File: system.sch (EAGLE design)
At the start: 24 parts, among them IC1 TPS7B8650BQDDARQ1, J1 163-179PH-EX, J2 TSW-104-07-F-S, U1 ATMEGA328PB-AU

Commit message: Removed redundant V_SIG to ADC line
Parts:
- removed R8: 0, rcl:R-US_R0603
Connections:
- removed net N$11: R8.1, U1.(ADC2/PTCY)PC2
- removed net V_SIG: R8.2
- net N$3: no longer R8.1
- net VS_5V: no longer R8.2
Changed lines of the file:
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@@
 <part name="R7" library="rcl" library_urn="urn:adsk.eagle:library:334" deviceset="R-US_" device="R0603" package3d_urn="urn:adsk.eagle:package:23555/3" value="0"/>
 <part name="X_10" library="ngspice-simulation" library_urn="urn:adsk.eagle:library:527439" deviceset="GND" device=""/>
-<part name="R8" library="rcl" library_urn="urn:adsk.eagle:library:334" deviceset="R-US_" device="R0603" package3d_urn="urn:adsk.eagle:package:23555/3" value="0"/>
 <part name="R9" library="rcl" library_urn="urn:adsk.eagle:library:334" deviceset="R-US_" device="R0603" package3d_urn="urn:adsk.eagle:package:23555/3" value="0"/>
 <part name="R10" library="rcl" library_urn="urn:adsk.eagle:library:334" deviceset="R-US_" device="R0603" package3d_urn="urn:adsk.eagle:package:23555/3" value="0"/>
@@
 </instance>
 <instance part="X_10" gate="G$1" x="-104.14" y="104.14" smashed="yes"/>
-<instance part="R8" gate="G$1" x="-60.96" y="0" smashed="yes">
-<attribute name="NAME" x="-64.262" y="1.2446" size="1.778" layer="95"/>
-<attribute name="VALUE" x="-64.008" y="-2.032" size="1.778" layer="96"/>
-</instance>
 <instance part="R9" gate="G$1" x="93.98" y="7.62" smashed="yes">
 <attribute name="NAME" x="90.17" y="9.1186" size="1.778" layer="95"/>
@@
 </segment>
 </net>
-<net name="N$11" class="0">
-<segment>
-<pinref part="R8" gate="G$1" pin="1"/>
-<pinref part="U1" gate="A" pin="(ADC2/PTCY)PC2"/>
-<wire x1="-66.04" y1="0" x2="-68.58" y2="0" width="0.1524" layer="91"/>
-</segment>
-</net>
-<net name="V_SIG" class="0">
-<segment>
-<pinref part="R8" gate="G$1" pin="2"/>
-<wire x1="-55.88" y1="0" x2="-38.1" y2="0" width="0.1524" layer="91"/>
-<label x="-38.1" y="0" size="1.778" layer="95"/>
-</segment>
-</net>

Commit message: Fixed warnings
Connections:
- net N$4: now also C2.1, L1.1, U1.AVCC
- net N$5: now also C2.1, C4.1, R7.1
- net VS_5V: no longer C2.1, L1.1, R7.1, U1.AVCC
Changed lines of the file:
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@@
 <port name="VS_5V" side="right" coord="5.08" direction="io"/>
 <port name="VS_2.5V" side="right" coord="-5.08" direction="io"/>
+<port name="VS_1.5V" side="right" coord="-15.24" direction="io"/>
 </ports>
 <variantdefs>
@@
 <net name="VS_5V" class="0">
 <segment>
-<pinref part="Q1" gate="G$1" pin="E"/>
-<wire x1="-15.24" y1="60.96" x2="-15.24" y2="58.42" width="0.1524" layer="91"/>
-<pinref part="C2" gate="G$1" pin="1"/>
-<wire x1="-15.24" y1="58.42" x2="-15.24" y2="55.88" width="0.1524" layer="91"/>
-<junction x="-15.24" y="58.42"/>
-<pinref part="R1" gate="G$1" pin="2"/>
-<wire x1="-15.24" y1="55.88" x2="-15.24" y2="51.816" width="0.1524" layer="91"/>
-<wire x1="-15.24" y1="55.88" x2="-22.86" y2="55.88" width="0.1524" layer="91"/>
-<junction x="-15.24" y="55.88"/>
-<wire x1="-22.86" y1="55.88" x2="-26.416" y2="55.88" width="0.1524" layer="91"/>
-<wire x1="-15.24" y1="58.42" x2="1.524" y2="58.42" width="0.1524" layer="91"/>
-<pinref part="C4" gate="G$1" pin="1"/>
-<wire x1="-22.86" y1="51.816" x2="-22.86" y2="55.88" width="0.1524" layer="91"/>
-<junction x="-22.86" y="55.88"/>
-<pinref part="R7" gate="G$1" pin="1"/>
-</segment>
-<segment>
 <pinref part="R3" gate="G$1" pin="2"/>
 <wire x1="58.42" y1="76.2" x2="58.42" y2="83.82" width="0.1524" layer="91"/>
@@
 </segment>
 <segment>
-<pinref part="R7" gate="G$1" pin="2"/>
-<wire x1="11.684" y1="58.42" x2="17.78" y2="58.42" width="0.1524" layer="91"/>
 <label x="22.86" y="58.42" size="1.778" layer="95"/>
 <pinref part="R8" gate="G$1" pin="2"/>
@@
 <wire x1="11.684" y1="30.48" x2="17.78" y2="30.48" width="0.1524" layer="91"/>
 <wire x1="17.78" y1="30.48" x2="17.78" y2="58.42" width="0.1524" layer="91"/>
+<pinref part="R7" gate="G$1" pin="2"/>
+<wire x1="17.78" y1="58.42" x2="11.684" y2="58.42" width="0.1524" layer="91"/>
 <junction x="17.78" y="58.42"/>
 </segment>
@@
 <pinref part="R8" gate="G$1" pin="1"/>
 <wire x1="-5.08" y1="30.48" x2="1.524" y2="30.48" width="0.1524" layer="91"/>
+</segment>
+</net>
+<net name="N$5" class="0">
+<segment>
+<pinref part="R7" gate="G$1" pin="1"/>
+<wire x1="1.524" y1="58.42" x2="-15.24" y2="58.42" width="0.1524" layer="91"/>
+<pinref part="Q1" gate="G$1" pin="E"/>
+<wire x1="-15.24" y1="58.42" x2="-15.24" y2="60.96" width="0.1524" layer="91"/>
+<pinref part="C2" gate="G$1" pin="1"/>
+<wire x1="-15.24" y1="58.42" x2="-15.24" y2="55.88" width="0.1524" layer="91"/>
+<junction x="-15.24" y="58.42"/>
+<pinref part="R1" gate="G$1" pin="2"/>
+<wire x1="-15.24" y1="55.88" x2="-15.24" y2="51.816" width="0.1524" layer="91"/>
+<wire x1="-26.416" y1="55.88" x2="-22.86" y2="55.88" width="0.1524" layer="91"/>
+<junction x="-15.24" y="55.88"/>
+<wire x1="-22.86" y1="55.88" x2="-15.24" y2="55.88" width="0.1524" layer="91"/>
+<wire x1="-22.86" y1="55.88" x2="-22.86" y2="51.816" width="0.1524" layer="91"/>
+<junction x="-22.86" y="55.88"/>
+<pinref part="C4" gate="G$1" pin="1"/>
 </segment>
 </net>
@@
 <part name="R4" library="rcl" library_urn="urn:adsk.eagle:library:334" deviceset="R-US_" device="R0603" package3d_urn="urn:adsk.eagle:package:23555/3" value="10000"/>
 <part name="R5" library="rcl" library_urn="urn:adsk.eagle:library:334" deviceset="R-US_" device="R0603" package3d_urn="urn:adsk.eagle:package:23555/3" value="10000"/>
-<part name="C2" library="rcl" library_urn="urn:adsk.eagle:library:334" deviceset="C-US" device="C0603" package3d_urn="urn:adsk.eagle:package:23616/2" value="100nF"/>
 <part name="R1" library="rcl" library_urn="urn:adsk.eagle:library:334" deviceset="R-US_" device="R0603" package3d_urn="urn:adsk.eagle:package:23555/3" value="100"/>
 </parts>
@@
 <attribute name="NAME" x="120.65" y="52.2986" size="1.778" layer="95"/>
 <attribute name="VALUE" x="120.65" y="47.498" size="1.778" layer="96"/>
-</instance>
-<instance part="C2" gate="G$1" x="63.5" y="-35.56" smashed="yes" rot="R90">
-<attribute name="NAME" x="62.865" y="-34.544" size="1.778" layer="95" rot="R90"/>
-<attribute name="VALUE" x="67.691" y="-34.544" size="1.778" layer="96" rot="R90"/>
 </instance>
 <instance part="R1" gate="G$1" x="60.96" y="63.5" smashed="yes">
@@
 </segment>
 </net>
-<net name="N$4" class="0">
-<segment>
-<wire x1="-69.85" y1="58.42" x2="-15.24" y2="58.42" width="0.1524" layer="91"/>
-<portref moduleinst="THERMISTOR_THERMOPILE" port="VS_2.5V"/>
-<portref moduleinst="LDO_AND_VOLTAGE_REFS" port="VS_2.5V"/>
-</segment>
-</net>
 <net name="VS_5V" class="0">
 <segment>
@@
 </segment>
 <segment>
-<pinref part="U1" gate="A" pin="AVCC"/>
-<wire x1="-68.58" y1="-17.78" x2="-60.96" y2="-17.78" width="0.1524" layer="91"/>
-<pinref part="C2" gate="G$1" pin="1"/>
-<wire x1="-60.96" y1="-17.78" x2="-60.96" y2="-20.32" width="0.1524" layer="91"/>
-<pinref part="L1" gate="G$1" pin="1"/>
-<wire x1="-60.96" y1="-17.78" x2="-58.42" y2="-17.78" width="0.1524" layer="91"/>
-<junction x="-60.96" y="-17.78"/>
-</segment>
-<segment>
 <portref moduleinst="LDO_AND_VOLTAGE_REFS" port="VS_5V"/>
 <pinref part="C4" gate="G$1" pin="1"/>
@@
 <pinref part="R10" gate="G$1" pin="1"/>
 </segment>
+<segment>
+<portref moduleinst="LDO_AND_VOLTAGE_REFS" port="VS_1.5V"/>
+<wire x1="-69.85" y1="48.26" x2="-60.96" y2="48.26" width="0.1524" layer="91"/>
+<label x="-60.96" y="48.26" size="1.778" layer="95"/>
+</segment>
 </net>
 <net name="VS_2.5V" class="0">
@@
 <wire x1="92.71" y1="66.04" x2="81.28" y2="66.04" width="0.1524" layer="91"/>
 <label x="81.28" y="66.04" size="1.778" layer="95" rot="R180"/>
+</segment>
+<segment>
+<wire x1="-69.85" y1="58.42" x2="-15.24" y2="58.42" width="0.1524" layer="91"/>
+<portref moduleinst="THERMISTOR_THERMOPILE" port="VS_2.5V"/>
+<portref moduleinst="LDO_AND_VOLTAGE_REFS" port="VS_2.5V"/>
+<label x="-60.96" y="58.42" size="1.778" layer="95" rot="R180"/>
 </segment>
 </net>
@@
 </segment>
 </net>
+<net name="N$4" class="0">
+<segment>
+<pinref part="L1" gate="G$1" pin="1"/>
+<pinref part="U1" gate="A" pin="AVCC"/>
+<wire x1="-58.42" y1="-17.78" x2="-60.96" y2="-17.78" width="0.1524" layer="91"/>
+<pinref part="C2" gate="G$1" pin="1"/>
+<wire x1="-60.96" y1="-17.78" x2="-68.58" y2="-17.78" width="0.1524" layer="91"/>
+<wire x1="-60.96" y1="-17.78" x2="-60.96" y2="-20.32" width="0.1524" layer="91"/>
+<junction x="-60.96" y="-17.78"/>
+</segment>
+</net>
 </nets>
 </sheet>
 </sheets>
+<errors>
+</errors>
 </schematic>
 </drawing>

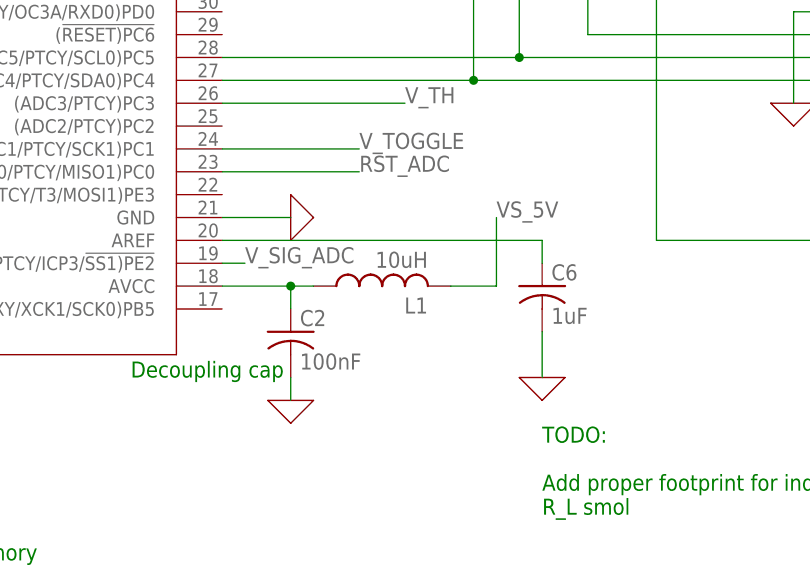
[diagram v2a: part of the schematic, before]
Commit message: added footprint for L AVCC
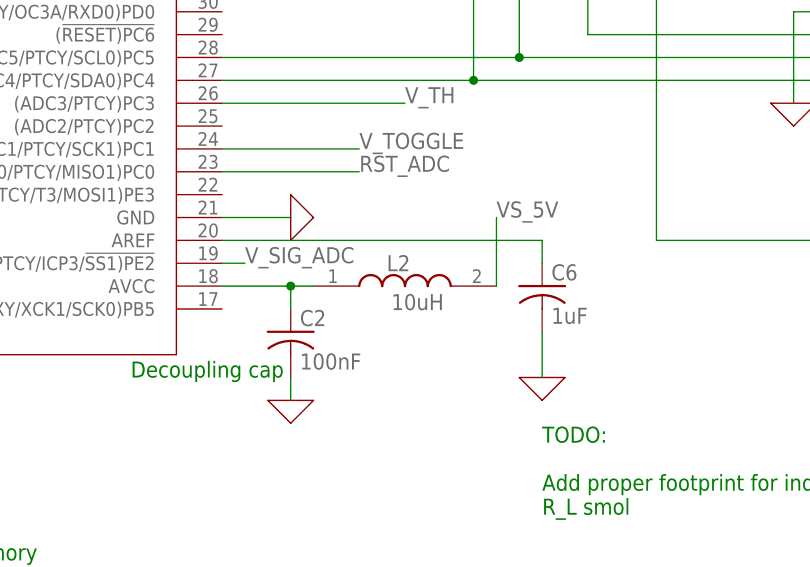
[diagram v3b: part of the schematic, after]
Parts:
- removed L1: 10uH, rcl:L-USIR-4
- added L2: 10uH, SRP1038CC-100M:SRP1038CC-100M
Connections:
- net N$2: no longer L1.1
- net N$4: now also L2.1; no longer L1.1
- net VS_5V: now also L2.2; no longer L1.2
- net VS_6V: no longer L1.2
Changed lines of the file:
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@@
 <part name="C6" library="rcl" library_urn="urn:adsk.eagle:library:334" deviceset="C-US" device="C0603" package3d_urn="urn:adsk.eagle:package:23616/2" value="1uF"/>
 <part name="X_4" library="ngspice-simulation" library_urn="urn:adsk.eagle:library:527439" deviceset="GND" device=""/>
-<part name="L1" library="rcl" library_urn="urn:adsk.eagle:library:334" deviceset="L-US" device="IR-4" package3d_urn="urn:adsk.eagle:package:23516/1" value="10uH"/>
 <part name="X_11" library="ngspice-simulation" library_urn="urn:adsk.eagle:library:527439" deviceset="GND" device=""/>
 <part name="R12" library="rcl" library_urn="urn:adsk.eagle:library:334" deviceset="R-US_" device="R0603" package3d_urn="urn:adsk.eagle:package:23555/3" value="0"/>
+<part name="L2" library="SRP1038CC-100M" deviceset="SRP1038CC-100M" device="" value="10uH"/>
 </parts>
 <sheets>
@@
 </instance>
 <instance part="X_4" gate="G$1" x="-33.02" y="-27.94" smashed="yes"/>
-<instance part="L1" gate="G$1" x="-50.8" y="-17.78" smashed="yes" rot="R90">
-<attribute name="NAME" x="-45.72" y="-19.05" size="1.778" layer="95" rot="R180"/>
-<attribute name="VALUE" x="-45.72" y="-13.97" size="1.778" layer="96" rot="R180"/>
-</instance>
 <instance part="X_11" gate="G$1" x="-60.96" y="-10.16" smashed="yes" rot="R90"/>
 <instance part="R12" gate="G$1" x="177.8" y="58.42" smashed="yes">
 <attribute name="NAME" x="173.99" y="59.9186" size="1.778" layer="95"/>
 <attribute name="VALUE" x="173.99" y="55.118" size="1.778" layer="96"/>
+</instance>
+<instance part="L2" gate="G$1" x="-58.42" y="-17.78" smashed="yes">
+<attribute name="NAME" x="-50.292" y="-15.24" size="1.778" layer="95" align="center-left"/>
+<attribute name="VALUE" x="-49.784" y="-19.558" size="1.778" layer="96" align="center-left"/>
 </instance>
 </instances>
@@
 </segment>
 <segment>
-<pinref part="L1" gate="G$1" pin="2"/>
-<wire x1="-43.18" y1="-17.78" x2="-38.1" y2="-17.78" width="0.1524" layer="91"/>
 <wire x1="-38.1" y1="-17.78" x2="-38.1" y2="-10.16" width="0.1524" layer="91"/>
 <label x="-38.1" y="-10.16" size="1.778" layer="95"/>
+<pinref part="L2" gate="G$1" pin="2"/>
 </segment>
 </net>
@@
 <net name="N$4" class="0">
 <segment>
-<pinref part="L1" gate="G$1" pin="1"/>
 <pinref part="U1" gate="A" pin="AVCC"/>
 <wire x1="-58.42" y1="-17.78" x2="-60.96" y2="-17.78" width="0.1524" layer="91"/>
@@
 <wire x1="-60.96" y1="-17.78" x2="-60.96" y2="-20.32" width="0.1524" layer="91"/>
 <junction x="-60.96" y="-17.78"/>
-</segment>
-</net>
+<pinref part="L2" gate="G$1" pin="1"/>
+</segment>
+</net>

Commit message: renamed voltage nets, cleaned up nets and module flow
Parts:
- added C7: 1uF, rcl:C-USC0603
- added IC2, IC4: TLV9101IDBVR, TLV9101IDBVR:TLV9101IDBVR
- added R13, R14: 2000000, rcl:R-US_R0603
- added R15, R16, R19, R20, R21, R8: 0, rcl:R-US_R0603
- added R17: 5000, rcl:R-US_R0603
- added R18: 1500, rcl:R-US_R0603
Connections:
- removed net N$12: R9.2
- removed net N$13: R10.2
- new net N$16: IC2.IN+, R13.1, R14.2
- new net N$8: IC4.IN-, R17.1, R18.2
- new net VS_1.5V_BACKUP: C7.1, IC4.OUT, R17.2, R20.2
- new net VS_1.5V_OUT: IC1.IN+, R10.2, R19.2, R20.1
- new net VS_2.5V_BACKUP: IC2.IN-, IC2.OUT, R16.2
- new net VS_2.5V_OUT: C5.1, C6.1, IC1.-IN, IC1.REF, IC2.THERMOPILE_GND, R15.2, R16.1
- new net VS_5V_BACKUP: C4.1, IC1.OUT, IC2.V+, IC4.V+, R13.2, R6.2, R8.2
- new net VS_5V_OUT: C1.1, IC1.+VS, IC1.V+, IC2.V+, IC4.VDD, J2.02, L2.2, R1.2, R2.2, R5.2, R8.1, R9.1, U1.VCC
- new net V_SIG: C7.2, IC2.IN-, IC2.OUT, R12.1, R21.1
- net 0: now also C7.2, IC2.THERMISTOR_GND, IC2.V-, IC4.GND, IC4.V-, R14.1, R18.1
- net N$2: now also IC2.IN+, R21.2; no longer R3.2
- net N$3: now also IC4.S2, R8.1
- net N$4: now also IC4.D
- net N$5: now also R10.1
- net N$6: now also C7.1, IC4.IN-, R9.2; no longer R12.1
- net N$7: now also IC2.IN+; no longer R3.1, R4.1
- net RST_ADC: now also IC4.SEL
- net VS_1.5V: now also IC4.OUT, R19.1; no longer IC1.IN+, R10.1
- net VS_2.5V: now also IC2.IN-, IC2.OUT, R15.1; no longer C5.1, C6.1, IC1.-IN, IC1.REF
- net VS_5V: now also IC2.V+, IC4.V+, R8.2; no longer C1.1, C4.1, IC1.+VS, IC1.OUT, IC1.V+, J2.02, L2.2, R1.2, R2.2, R5.2, R6.2, R9.1, U1.VCC
- net VS_6V: now also R3.1, R4.1
- net V_BG: now also IC4.IN+
- net V_TH: now also IC2.THERMISTOR
- net V_TP: now also IC2.THERMOPILE
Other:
- note added: "ADC RST SWITCH"
- note added: "ADC SWITCH"
- note added: "Cut power to backup LDO"
- note added: "Cut power to our LDO"
- note added: "Output"
- note added: "RST_ADC and V_TOGGLE from MCU"
- note added: "V_SIG_ADC: backup to connect thermopile to ADC"
- moved on the sheet: C1, C2, C3, C4, C5, C6, FUSE, IC1, J1, J2, L2, R1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

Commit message: renamed parts on main sheet
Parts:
- removed IC4: TLV9101IDBVR, TLV9101IDBVR:TLV9101IDBVR
- removed L2: 10uH, SRP1038CC-100M:SRP1038CC-100M
- added IC3: TLV9101IDBVR, TLV9101IDBVR:TLV9101IDBVR
- added L1: 10uH, SRP1038CC-100M:SRP1038CC-100M
- C2: value 100nF -> 1uF
- C3: value 1uF -> 22uF
- C4: value 22uF -> 100nF
- J1: value 163-179PH-EX -> TSW-104-07-F-S; device 163-179PH-EX:163-179PH-EX -> TSW-104-07-F-S:TSW-104-07-F-S
- J2: value TSW-104-07-F-S -> 163-179PH-EX; device TSW-104-07-F-S:TSW-104-07-F-S -> 163-179PH-EX:163-179PH-EX
- R1, R2: value 2000 -> 0
- R13, R14: value 2000000 -> 0
- R17: value 5000 -> 0
- R18: value 1500 -> 0
- R20: value 0 -> 5000
- R21: value 0 -> 1500
- R5, R6: value 0 -> 2000
- R7, R8: value 0 -> 2000000
- renumbered FUSE to F11
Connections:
- net 0: now also IC3.V-, J1.01, J2.B, J2.C, R21.1, R8.1; no longer IC4.GND, IC4.V-, J1.B, J1.C, J2.01, R14.1, R18.1, R7.1
- net ADC_EXT_INT: now also IC3.OUT, R12.2; no longer R11.2
- net N$10: now also R3.1, R4.2; no longer R6.1, R7.2
- net N$14: now also R12.1; no longer R11.1
- net N$16: now also R7.1, R8.2; no longer R13.1, R14.2
- net N$2: now also L1.1, R16.2; no longer R21.2
- net N$3: now also J2.A; no longer IC4.S2, J1.A
- net N$4: now also C4.1, IC3.IN+, L1.1; no longer C2.1, IC4.D, L2.1
- net N$5: now also R18.1; no longer R10.1
- net N$6: now also R17.2; no longer IC4.IN-, R9.2
- net N$8: now also IC3.IN-, R20.1, R21.2; no longer IC4.IN-, R17.1, R18.2
- net N$9: now also C2.1, R1.2; no longer C5.1, R4.2
- net RST_ADC: no longer IC4.SEL
- net SCL: now also J1.03, R6.1; no longer J2.03, R1.1
- net SDA: now also J1.04, R5.1; no longer J2.04, R2.1
- net VS_1.5V: now also R11.1; no longer IC4.OUT, R19.1
- net VS_1.5V_BACKUP: now also IC3.OUT, R15.2; no longer IC4.OUT, R17.2
- net VS_1.5V_OUT: now also IC3.IN-, R11.2, R15.1, R18.2; no longer R10.2, R19.2, R20.1
- net VS_2.5V: now also R10.1; no longer R15.1
- net VS_2.5V_BACKUP: now also R14.2; no longer R16.2
- net VS_2.5V_OUT: now also R10.2, R14.1; no longer R15.2, R16.1
- net VS_5V: now also R9.1; no longer IC4.V+, R5.1
- net VS_5V_BACKUP: now also C5.1, IC3.V+, R3.2, R7.2; no longer C4.1, IC4.V+, R6.2, R8.2
- net VS_5V_OUT: now also IC3.V+, J1.02, L1.2, R13.1, R17.1, R6.2, R9.2; no longer IC4.VDD, J2.02, L2.2, R2.2, R8.1, R9.1
- net VS_6V: now also L1.2, R1.1, R2.1; no longer R3.1, R4.1
- net V_BG: now also IC3.IN+; no longer IC4.IN+
- net V_SIG: now also R16.1, R19.1; no longer R12.1, R21.1
- net V_SIG_ADC: now also R19.2; no longer R12.2
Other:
- moved on the sheet: C2, C3, C4, C5, R1, R10, R11, R12, R13, R14, R15, R16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

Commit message: validated AMP_AND_FILTER block. fixed wiring on DUAL_SLOPE_ADC
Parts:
- R5, R6: value 2000 -> 10000
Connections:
- net ADC_EXT_INT: now also R2.2
- net N$1: now also R1.2; no longer R3.2
- net N$2: now also C1.2, IC1.OUT, IC3.IN+
- net N$3: no longer C1.2, IC1.OUT
- net N$4: no longer IC3.IN+
- net VS_2.5V_OUT: now also C6.2; no longer C6.1
- net VS_5V_OUT: now also C2.1, R2.1
- net V_TP: now also C6.1; no longer C6.2
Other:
- note added: "Instrumentation Amp with 495 gain"
- note added: "Open-drain output"
- note added: "Second order sallen key filter with 18.9Hz cutoff, no gain"
- note removed: "Instrumentation Amp with 500 gain"
- note removed: "Second order sallen key filter with 20Hz cutoff, no gain"
